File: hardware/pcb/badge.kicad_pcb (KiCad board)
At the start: 2 copper layers, 91 x 84 mm, 57 parts, among them J1 EPD FPC 24P 0.5mm, J2 BATT JST-SH 1.0mm, J3 USB-C 16P 沉板 (TYPE-C-31-M-14), Q1 AO3400A, Q2 AO3401A, SW1 RESET, SW2 BOOT/USER, U1 ESP32-C3-MINI-1-N4, U2 ST25DV64KC-IER6S3, U3 TP4054 / MCP73831T-2ACI/OT, U4 XC6220B331MR-G

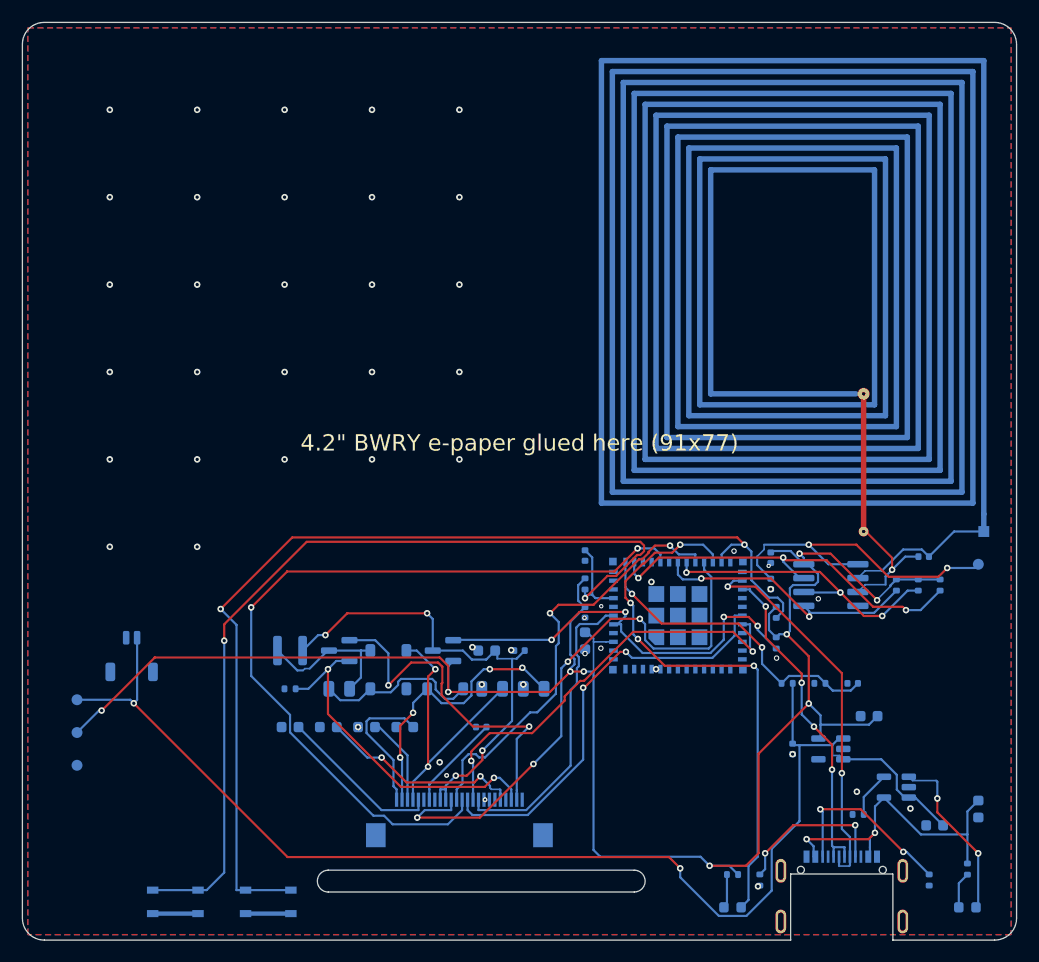
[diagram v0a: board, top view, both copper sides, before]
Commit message: Land H2 board (KiCad 10 full ERC/DRC 0) and firmware v0.2 F1.
Freeze the 680/115 board, hygiene scripts, and self-test fixes (GPIO1 wake, serial W, BUSY fail-closed) so GitHub matches the local pass. v0.1 bins stay as baseline.

Co-authored-by: Cursor <cursoragent@cursor.com>
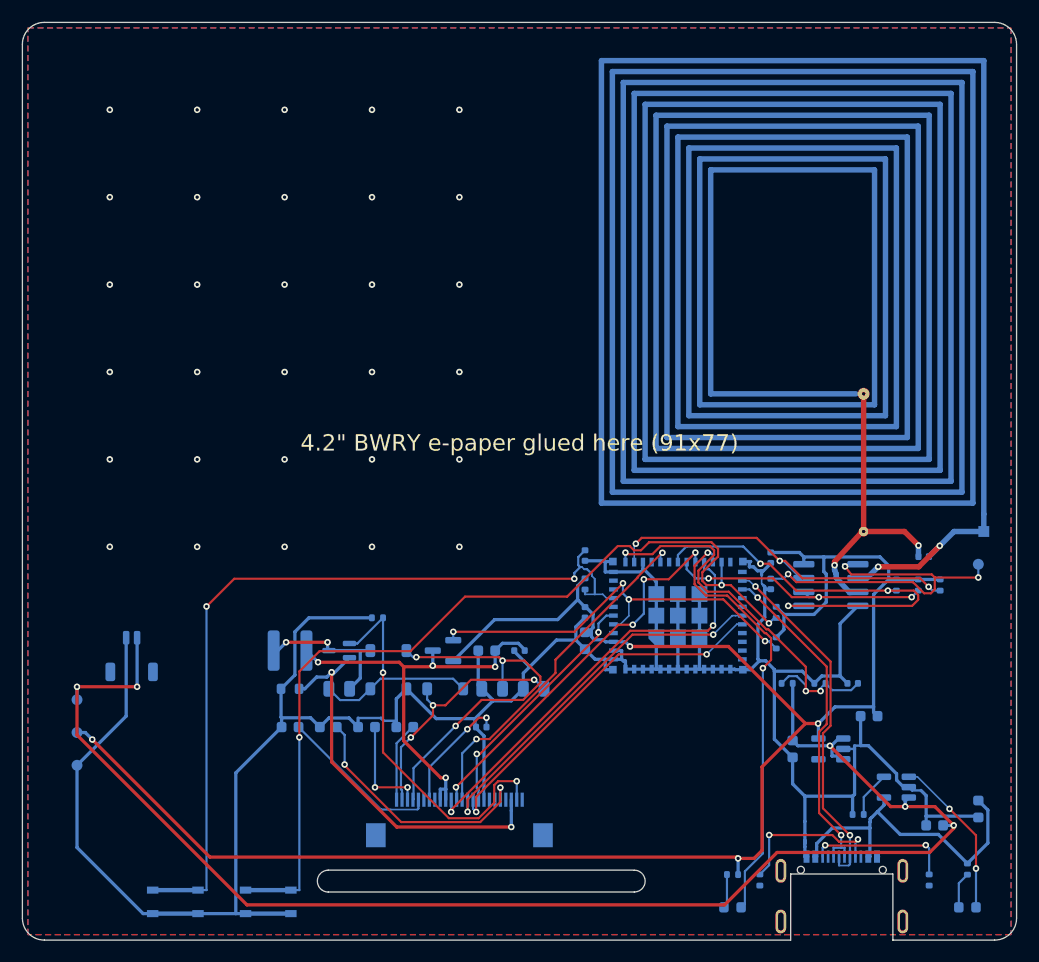
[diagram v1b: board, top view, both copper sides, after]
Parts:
- added R15: 1M, Resistor_SMD:R_0402_1005Metric, B.Cu at (32.5, 54.5)
- ANT1: footprint NFC_Loop -> badge:NFC_Loop
- C1, C12, C18, C19, C2, C20, C21, C6: footprint C_0603_1608Metric -> Capacitor_SMD:C_0603_1608Metric
- C10, C11, C13, C14, C5, C7, C8, C9: footprint C_0402_1005Metric -> Capacitor_SMD:C_0402_1005Metric
- C15: value 1u/50V -> 4.7u/25V; footprint C_0805_2012Metric -> Capacitor_SMD:C_0805_2012Metric
- C16, C17: footprint C_0805_2012Metric -> Capacitor_SMD:C_0805_2012Metric
- C3: value 1u -> 10u; footprint C_0402_1005Metric -> Capacitor_SMD:C_0603_1608Metric
- C4: value 2.2u -> 4.7u; footprint C_0603_1608Metric -> Capacitor_SMD:C_0603_1608Metric
- D1, D2, D3: footprint D_SOD-123 -> Diode_SMD:D_SOD-123
- D4, D5: footprint LED_0603_1608Metric -> LED_SMD:LED_0603_1608Metric
- J1: footprint Hirose_FH12-24S-0.5SH_1x24-1MP_P0.50mm_Horizontal -> Connector_FFC-FPC:Hirose_FH12-24S-0.5SH_1x24-1MP_P0.50mm_Horizontal
- J2: value BATT JST-SH 1.0mm -> BATT JST-SHL 1.0mm; footprint JST_SHL_SM02B-SHLS-TF_1x02-1MP_P1.00mm_Horizontal -> badge:JST_SHL_SM02B-SHLS-TF_1x02-1MP_P1.00mm_Horizontal
- J3: footprint TYPE-C-31-M-14 -> badge:TYPE-C-31-M-14
- L1: value 68uH -> 47uH; footprint L_Changjiang_FNR3015S -> Inductor_SMD:L_Changjiang_FNR4018S
- Q1: value AO3400A -> Si1308EDL; footprint SOT-23 -> badge:SOT-323_SC-70
- Q2: footprint SOT-23 -> Package_TO_SOT_SMD:SOT-23
- R1, R10, R11, R12, R13, R2, R3, R4, R5, R6, R7, R8, R9: footprint R_0402_1005Metric -> Resistor_SMD:R_0402_1005Metric
- R14: footprint R_0402_1005Metric -> Resistor_SMD:R_0603_1608Metric
- SW1, SW2: footprint SW_SPST_PTS810 -> Button_Switch_SMD:SW_SPST_PTS810
- TP1, TP2, TP3, TP4: footprint TestPoint_Pad_D1.0mm -> TestPoint:TestPoint_Pad_D1.0mm
- U1: footprint ESP32-C3-MINI-1 -> badge:ESP32-C3-MINI-1
- U2: footprint SOIC-8_3.9x4.9mm_P1.27mm -> Package_SO:SOIC-8_3.9x4.9mm_P1.27mm
- U3: value TP4054 / MCP73831T-2ACI/OT -> TP4054; footprint SOT-23-5 -> Package_TO_SOT_SMD:SOT-23-5
- U4: footprint SOT-23-5 -> Package_TO_SOT_SMD:SOT-23-5
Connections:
- J1 pad 1: (no net) -> unconnected-(J1-Pin_1-Pad1)
- J1 pad 19: (no net) -> unconnected-(J1-Pin_19-Pad19)
- J1 pad 4: (no net) -> unconnected-(J1-Pin_4-Pad4)
- J1 pad 6: (no net) -> unconnected-(J1-Pin_6-Pad6)
- J1 pad 7: GND -> unconnected-(J1-Pin_7-Pad7)
- J3 pad A8: (no net) -> unconnected-(J3-SBU1-PadA8)
- J3 pad B8: (no net) -> unconnected-(J3-SBU2-PadB8)
- U1 pad 10: (no net) -> unconnected-(U1-NC-Pad10)
- U1 pad 15: (no net) -> unconnected-(U1-NC-Pad15)
- U1 pad 17: (no net) -> unconnected-(U1-NC-Pad17)
- U1 pad 24: (no net) -> unconnected-(U1-NC-Pad24)
- U1 pad 25: (no net) -> unconnected-(U1-NC-Pad25)
- U1 pad 28: (no net) -> unconnected-(U1-NC-Pad28)
- U1 pad 29: (no net) -> unconnected-(U1-NC-Pad29)
- U1 pad 32: (no net) -> unconnected-(U1-NC-Pad32)
- U1 pad 33: (no net) -> unconnected-(U1-NC-Pad33)
- U1 pad 34: (no net) -> unconnected-(U1-NC-Pad34)
- U1 pad 35: (no net) -> unconnected-(U1-NC-Pad35)
- U1 pad 4: (no net) -> unconnected-(U1-NC-Pad4)
- U1 pad 7: (no net) -> unconnected-(U1-NC-Pad7)
- U1 pad 9: (no net) -> unconnected-(U1-NC-Pad9)
- U4 pad 4: (no net) -> unconnected-(U4-NC-Pad4)
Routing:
- net GND: track 8.30 -> 265.1 mm, vias 50 -> 30
- net EPD_CS: track 74.3 -> 31.9 mm
- net VBAT: track 118.7 -> 134.2 mm, vias 2 -> 5
- net I2C_SDA: track 24.8 -> 39.6 mm, vias 2 -> 3
- net EPD_MOSI: track 52.5 -> 38.8 mm, vias 4 -> 2
- net EN: track 87.2 -> 75.3 mm
- net BOOT_n: track 94.3 -> 83.0 mm, vias 2 -> 3
- net LED_STAT_n: track 50.7 -> 39.4 mm, vias 4 -> 2
- net BAT_SENSE: track 29.2 -> 37.4 mm, vias 2 -> 3
- net EPD_VGH: track 26.1 -> 34.1 mm, vias 2 -> 3
- net EPD_VCOM: track 13.0 -> 7.31 mm
- net EPD_RST: track 39.0 -> 33.5 mm
- net EPD_BUSY: track 28.0 -> 22.7 mm, vias 0 -> 2
- net EPD_SCK: track 39.9 -> 34.7 mm, vias 2 -> 4
- net EPD_DC: track 39.2 -> 34.4 mm
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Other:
- board text added: "J2-1 VBAT"
